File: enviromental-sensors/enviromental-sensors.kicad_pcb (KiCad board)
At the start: 2 copper layers, 77.9 x 45.2 mm, 45 parts, among them IC1 ESP32-C3-WROOM-02-N4, IC2 TPS2117DRLR, J1 USB_C_Receptacle_USB2.0, J2 S2B-PH-SM4-TB_LF__SN_, J3 FH52-10S-0.5SH_99, J4 Conn_01x02_Socket, Q1 AO3401A, SW1 TC-0522C-1.7-160G, SW2 TC-0522C-1.7-160G, SW3 TC-0522C-1.7-160G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

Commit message: Add env. sensors PCB
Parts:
- removed TP1: U3EN, TestPoint:TestPoint_Pad_D1.5mm
- removed TP2: U4EN, TestPoint:TestPoint_Pad_D1.5mm
- removed U3: LP5240HVF, footprint:C2890373_WLCSP-4
- added J5: SM04B-SRSS-TB_LF__SN_, enviromental:QWIIC_SM04B-SRSS-TB_LFSN_, F.Cu at (171.9, 68.0)
- added Q2: TEMT6000X01, enviromental:TEMT6000X01, F.Cu at (134.8, 58.4)
- added Q3: TEMT6000X01, enviromental:TEMT6000X01, B.Cu at (131.8, 55.4)
- added U5: SCD40-D-R2, Sensor:Sensirion_SCD4x-1EP_10.1x10.1mm_P1.25mm_EP4.8x4.8mm, F.Cu at (123.8, 57.9)
- R14: value r=0 -> 0Ω
- SW3: value TC-0522C-1.7-160G -> K2-1806SQ-A2DW-04; footprint footprint:C2845289_SW-SMD_4P-L5.2-W5.2-P3.70-LS6.4 -> enviromental:C5143621_KEY-SMD_TS24ZJ
- U2: value MCP1700-3302E_SOT23 -> RT9080-33GJ5; footprint Package_TO_SOT_SMD:SOT-23 -> Package_TO_SOT_SMD:TSOT-23-5
- U4: value LP5240HVF -> AP22811; footprint footprint:C2890373_WLCSP-4 -> enviromental:C3001660_SOT95P285X140-5N
- moved SW3 4.85 mm to (111.6, 84.0), turned to 90 degrees
- moved U4 2.67 mm to (135.2, 98.0), turned to 45 degrees
- moved U2 0.19 mm to (130.2, 101.7), turned to 45 degrees
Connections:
- D1 pad 1: Net-(D1-K) -> PWR_STAT
- IC1 pad 16: /LCD_CS -> /LIGHT_MEASURE
- IC1 pad 7: PWR_STAT -> /LCD_CS
- R11 pad 1: Net-(D1-K) -> PWR_STAT
- R13 pad 2: Net-(D1-K) -> PWR_STAT
- SW3 pad 2: +3.3VP -> MCU_PWRHOLD
- SW3 pad 3: MCU_PWRHOLD -> unconnected-(SW3-Pad3)_1
- SW3 pad 4: MCU_PWRHOLD -> unconnected-(SW3-Pad4)
- U2 pad 1: GND -> +VDC
- U2 pad 2: +3.3V -> GND
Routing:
- net +3.3V: track 81.6 -> 171.7 mm, vias 0 -> 7
- net SCL: track 34.6 -> 93.1 mm, vias 2 -> 3
- net /LIGHT_MEASURE: track 0.00 -> 55.7 mm, vias 0 -> 1
- net SDA: track 34.9 -> 87.1 mm, vias 2 -> 3
- net GND: track 62.9 -> 77.2 mm, vias 29 -> 33
- net Net-(D1-K): track 12.2 -> 0.00 mm, vias 2 -> 0
- net /LCD_CS: track 32.0 -> 21.8 mm, vias 0 -> 2
- net PWR_STAT: track 61.1 -> 51.8 mm
- net VIN: track 53.1 -> 45.6 mm
- net MCU_PWRHOLD: track 42.6 -> 43.7 mm
- net +3.3VP: track 118.8 -> 119.7 mm
- net +VDC: track 13.5 -> 14.1 mm, vias 2 -> 0
- net /EN: vias 0 -> 2
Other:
- board size 77.9 x 45.2 mm -> 77.9 x 63.3 mm
- board text added: "3.3v"
- board text added: "CO2"
- board text added: "GND"
- board text added: "Rel 1.0"
- board text added: "SCL"
- board text added: "SDA"
- board text added: "enviromental"
- board text added: "sensors"
- board text removed: "LowPow"
- board text removed: "RTCINT Wake up"
- board text removed: "USB always on"
- board text removed: "experi"
- board text removed: "ment"

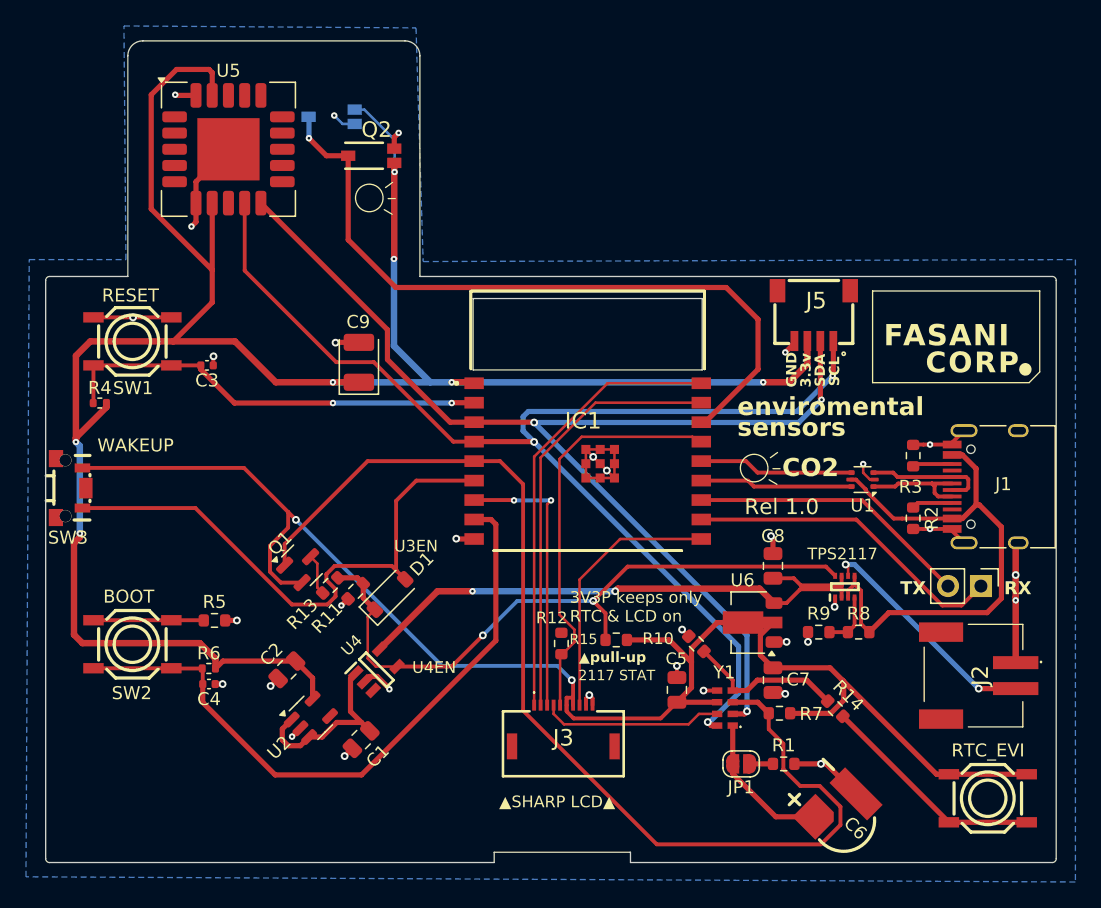
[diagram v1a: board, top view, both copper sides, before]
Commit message: 1.0 fixes: QWIIC corrected (note 1.0 release before this commit is unfixed)
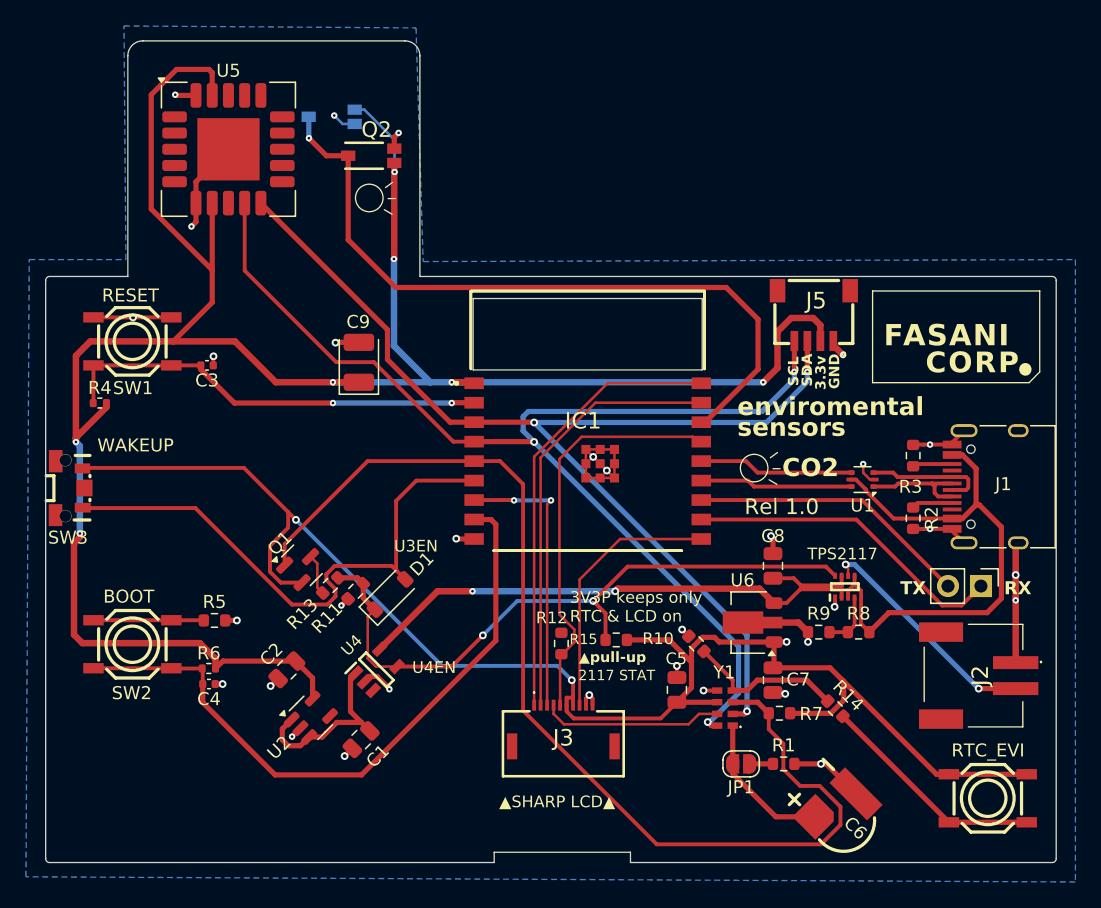
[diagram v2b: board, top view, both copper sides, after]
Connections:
- J5 pad 1: SCL -> GND
- J5 pad 2: SDA -> +3.3V
- J5 pad 3: +3.3V -> SDA
- J5 pad 4: GND -> SCL
- U6 pad 1: GND -> +3.3VP
- U6 pad 2: +3.3VP -> GND
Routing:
- net +3.3V: track 171.7 -> 175.4 mm
- net SCL: track 93.1 -> 90.3 mm
- net GND: track 77.2 -> 79.5 mm, vias 33 -> 32
- net SDA: track 87.1 -> 85.1 mm
- net +3.3VP: track 119.7 -> 118.1 mm, vias 2 -> 3
